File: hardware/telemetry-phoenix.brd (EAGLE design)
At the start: 100 x 80 mm, 134 parts, among them IC1 COPERNICUSSMD, IC10 TPS70933, IC2 TPS70933, IC4 STM32L052C8T6, IC5 TPS62160, IC6 HX1, IC7 LMP7702, IC8 ADXL345, J1 I2C1, J11 DNP, J13 LORA, J2 RASPBERRYPI-GPIOPTH, J5 BAT, J6 SMA_EDGE, J7 SMA_EDGE, J8 TEMP_E, Q1 SI4202DY, U1 VN5160S-E, U2 BME280, U3 VN5160S-E, Y1 32768, Y2 8M

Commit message: Add Phoenix telemetry PCB
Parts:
- removed C15, C27, C35: 1u, SparkFun-Passives:0805
- removed C17, C30: 0.1u, SparkFun-Passives:0805
- removed IC1: COPERNICUSSMD, SparkFun-RF:COPERNICUS
- removed J1: I2C1, SparkFun-Connectors:1X04_NO_SILK
- removed J13: LORA, HAB:1X08-2MM
- removed J5: BAT, SparkFun-Connectors:1X02
- removed J7: SMA_EDGE, SparkFun-Connectors:SMA-EDGE
- removed J8: TEMP_E, SparkFun-Connectors:JST-3-PTH
- removed JP1: GND, SparkFun-Passives:PAD-JUMPER-2-NC_BY_TRACE_YES_SILK
- removed OK1, OK2, OK3: LTV826S, optocoupler:DIL8-SMD
- removed R10\, R40: 430K, SparkFun-Passives:0805
- removed R2: 10K, SparkFun-Passives:0603-ARV
- removed R24, R42: 10K, SparkFun-Passives:0805
- removed R31, R33, R34, R35, R36, R37, R38, R39: 4.7K, SparkFun-Passives:0805
- removed R41: 100K, SparkFun-Passives:0805
- removed U1, U3: VN5160S-E, HAB:SO8
- removed U2: BME280, BME280ComponentLibrary:BME280_LGA
- added D11: 5.6V, SparkFun-DiscreteSemi:SOD-323
- added D15: 15V, SparkFun-DiscreteSemi:SOD-323
- added IC11, IC9: VN5160S-E, HAB:SO8
- added IC3: BME280, BME280ComponentLibrary:BME280_LGA
- added J3: POWER, HAB:1X10_SCREW
- added J4: GPS2, SparkFun-Connectors:1X06-1MM
- added J9: IO, SparkFun-Connectors:2X8
- added R56: 470K, SparkFun-Passives:0805
- D12: value 15V -> 5.6V
- J2: value RASPBERRYPI-GPIOPTH -> RASPBERRYPI-GPIO; device SparkFun-Boards:2X13-SHROUDED -> HAB:2X13-PI
- R10: value 470K -> 430K
- R21, R29, R30: value 4.7K -> 100
- R25, R4: value 10K -> 100
- R27: value 330k -> 330K
- R28: value 0 -> 100
- R32: value 4.7K -> DNP
- Y2: device SparkFun-FreqCtrl:HC49UP -> SparkFun-FreqCtrl:CRYSTAL-TXC-7A
- moved R50 277.0 mm to (53.3, 36.8)
- moved C29 257.0 mm to (46.4, 27.3), turned to 180 degrees
- moved R48 253.2 mm to (24.1, 40.0), turned to 180 degrees
- moved D13 252.9 mm to (54.6, 46.4), turned to 180 degrees
- moved R49 248.3 mm to (27.3, 26.7), turned to 180 degrees
- moved R51 247.7 mm to (4.45, 40.0)
- moved FRAME3 246.2 mm to (2.54, 57.1)
- moved C28 244.9 mm to (7.62, 48.9)
- moved R46 244.0 mm to (47.0, 52.7), turned to 180 degrees
- moved R47 243.9 mm to (47.0, 48.9), turned to 180 degrees
- moved R44 237.5 mm to (47.0, 50.8)
- moved R45 237.2 mm to (47.0, 47.0)
- moved Q1 235.2 mm to (53.3, 50.2), turned to 270 degrees
- moved R43 209.3 mm to (20.3, 48.3), turned to 270 degrees
- moved D12 190.5 mm to (12.7, 3.81), turned to 90 degrees
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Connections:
- net N$1 renamed CRB
- net N$2 renamed ACB
- removed net 15V: C29.1, R40.2, U3.5, U3.8
- removed net AGND: IC1.2, IC1.4, J7.GND@0, J7.GND@1, J7.GND@2, J7.GND@3, JP1.1
- removed net GPSBOOT: IC1.10, R4.1
- removed net L1+: R29.2
- removed net L1-: OK1.2
- removed net L2+: R31.2
- removed net L2-: OK2.2
- removed net L3+: R33.2
- removed net L3-: OK3.2
- removed net L4: OK1.3, R35.1
- removed net L4+: R35.2
- removed net L4-: OK1.4
- removed net L5: OK2.3, R37.1
- removed net L5+: R37.2
- removed net L5-: OK2.4
- removed net L6: OK3.3, R39.1
- removed net L6+: R39.2
- removed net L6-: OK3.4
- removed net LED4: IC4.28, OK1.6, R34.1
- removed net LED5: IC4.29, OK2.6, R36.1
- removed net LED6: IC4.32, OK3.6, R38.1
- removed net LP-: IC7.6, R28.1
- removed net PPS: IC1.19
- removed net RF_GPS: IC1.3, J7.SIG
- removed net RXA: IC1.21, R2.7
- removed net TXA: IC1.23, R2.6
- removed net VRAD: IC4.11, R40.1, R41.2
- removed net XRESET: IC1.11, R24.2
- removed net XSTBY: IC1.16, IC4.20, R25.2
- new net +9V: J3.6, J3.7, J3.8
- new net 3V_PI: J2.1
- new net 3V_PI2: J2.17
- net 15V_OUT: now also IC11.6, IC11.7, J3.4; no longer U3.6, U3.7
- net 3.3V: now also D12.C, J9.7, J9.8; no longer C11.1, C12.1, C15.1, C16.1, D10.C, IC1.12, J1.2, J13.7, J13.8, J2.1, J2.17, R2.2, R2.3, R2.4, R21.2, R24.1, R25.1, R30.2, R34.2, R36.2, R38.2, R4.2, R42.2, U2.P$2, U2.P$6, U2.P$8
- net 5V: now also IC9.5, IC9.8, J4.2, R10.2; no longer C17.1, R10\.2, U1.5, U1.8
- net 5V_PI: now also IC9.6, IC9.7; no longer C27.1, U1.6, U1.7
- net A-: now also R56.2; no longer R10.2
- net ALT_CTRL: now also J3.9
- net BME_SDO: now also IC3.P$5; no longer U2.P$5
- net B_LORA: now also D10.C, J9.14; no longer J13.3
- net B_MISO: now also J9.10, R28.1; no longer J13.6
- net B_MOSI: now also J9.6, R25.1; no longer J13.2
- net B_SCK: now also J9.12, R4.1; no longer J13.4
- net CUT_ROPE: now also D15.C, J3.10; no longer D12.C
- net D_PI: now also IC9.4; no longer U1.4
- net D_RAD: now also IC11.4; no longer U3.4
- net FB5: now also R10.1; no longer R10\.1
- net GND: now also D11.A, D15.A, IC11.1, IC3.P$1, IC3.P$7, IC9.1, J3.2, J3.3, J3.5, J4.1, J4.5, J9.15, J9.16, J9.9, R56.1; no longer C11.2, C12.2, C15.2, C17.2, C27.2, C30.2, C35.2, IC1.1, IC1.13, IC1.14, IC1.15, IC1.27, IC1.28, J1.1, J13.1, J13.5, J5.1, J8.2, JP1.2, OK1.5, OK1.7, OK2.5, OK2.7, OK3.5, OK3.7, R10.1, R41.1, U1.1, U2.P$1, U2.P$7, U3.1
- net GPSRX: no longer IC1.24, R2.5
- net GPSRX2: now also J4.4
- net GPSTX: no longer IC1.20
- net GPSTX2: now also J4.3
- net K_PI: now also IC4.10, IC9.2; no longer IC4.15, U1.2
- net K_RAD: now also IC11.2, IC4.29; no longer IC4.13, U3.2
- net L1: now also J9.2, R21.1; no longer OK1.1, R29.1
- net L2: now also J9.1, R29.1; no longer OK2.1, R31.1
- net L3: now also J9.4, R30.1; no longer OK3.1, R33.1
- net LED1: now also IC4.13, R21.2; no longer IC4.25, OK1.8, R21.1
- net LED2: now also IC4.12, R29.2; no longer IC4.26, OK2.8, R30.1
- net LED3: now also IC4.11, R30.2; no longer IC4.27, OK3.8, R32.1
- net LS1: now also J2.22; no longer J2.18
- net LS2: now also J2.18; no longer J2.22
- net MISO: now also R28.2
- net MOSI: now also R25.2
- net OSC_IN: now also Y2.P$1; no longer Y2.1
- net OSC_OUT: now also Y2.P$2; no longer Y2.2
- net R_TX: no longer R42.1
- net SCK: now also R4.2
- net SCL: now also IC3.P$4, J9.5; no longer J1.4, U2.P$4
- net SDA: now also IC3.P$3, J9.3; no longer J1.3, U2.P$3
- net TEMP: now also IC4.28, J9.13, R32.1; no longer IC4.10, J8.3
- net TXD: now also IC7.6; no longer R28.2
- net VBAT: now also C29.1, IC11.5, IC11.8, J3.1; no longer J5.2
- net VDIV: now also IC4.15; no longer IC4.12
- net VS: now also C16.1, D11.C, IC3.P$2, IC3.P$6, IC3.P$8, J9.11; no longer C30.1, C35.1, J8.1
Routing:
- net 3.3V: track 0.00 -> 93.1 mm
- net SCL: track 0.00 -> 78.1 mm, vias 0 -> 4
- net SDA: track 0.00 -> 77.5 mm, vias 0 -> 3
- net VS: track 0.00 -> 62.2 mm
- net K_RAD: track 0.00 -> 48.1 mm, vias 0 -> 2
- net !RST!: track 0.00 -> 40.2 mm, vias 0 -> 2
- net R_RX: track 0.00 -> 38.5 mm, vias 0 -> 1
- net LED2: track 0.00 -> 34.1 mm, vias 0 -> 2
- net GPSRX2: track 0.00 -> 33.8 mm, vias 0 -> 2
- net TEMP: track 0.00 -> 33.5 mm, vias 0 -> 2
- net K_PI: track 0.00 -> 33.4 mm, vias 0 -> 2
- net LED1: track 0.00 -> 33.2 mm, vias 0 -> 2
- net LED3: track 0.00 -> 33.1 mm, vias 0 -> 2
- net GPSTX2: track 0.00 -> 32.9 mm, vias 0 -> 2
- net MOSI: track 0.00 -> 30.7 mm, vias 0 -> 2
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- added copper zone on layer 1, net 15V_OUT
- added copper zone on layer 1, net 3.3V
- added copper zone on layer 1, net 5V
- added copper zone on layer 16, net 5V
- added copper zone on layer 1, net 5V_PI
- added copper zone on layer 1, net ALT_CTRL
- added copper zone on layer 1, net CUT_ROPE
- added copper zone on layer 1, net GND
- added copper zone on layer 16, net GND
- added copper zone on layer 1, net RGND
- added copper zone on layer 16, net RGND
- added copper zone on layer 1, net SW5
- added copper zone on layer 1, net VBAT
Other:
- board size 100 x 80 mm -> 65 x 56 mm

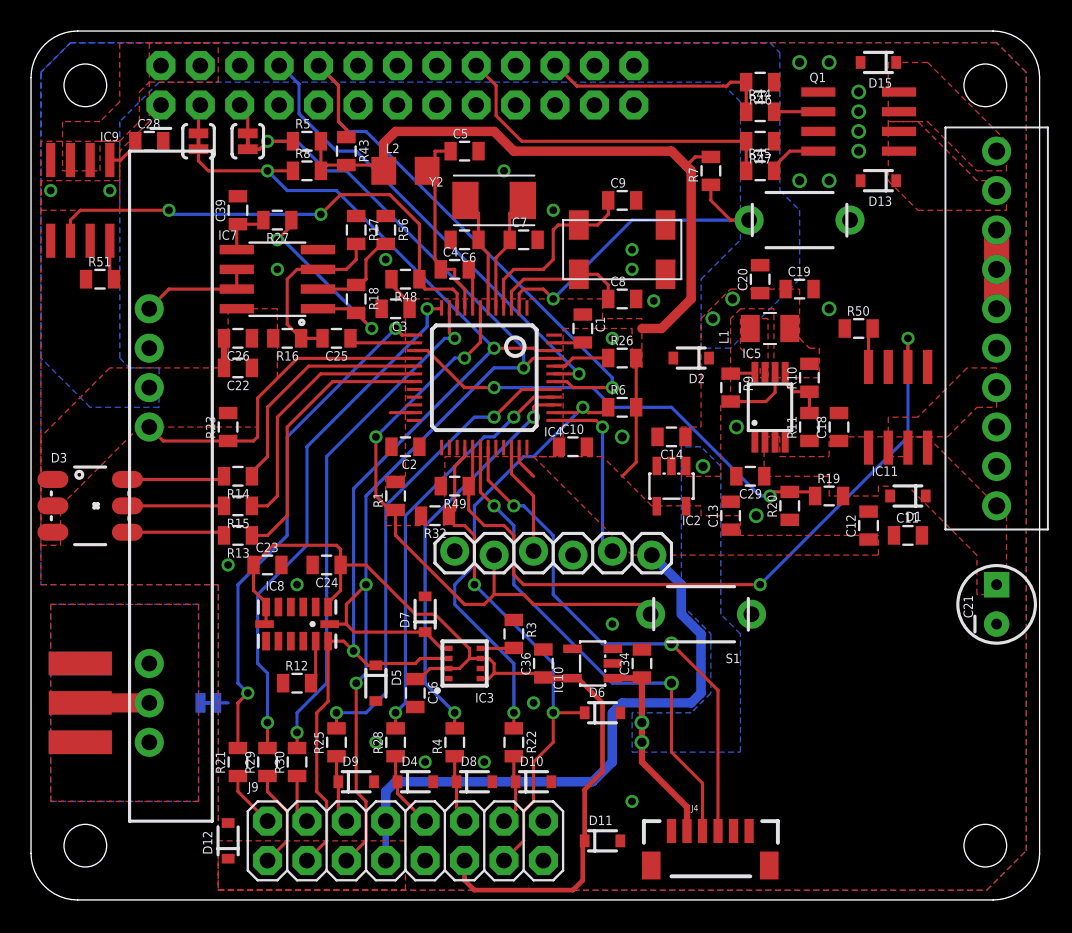
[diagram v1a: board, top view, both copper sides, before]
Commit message: Add GPS1 connector to Phoenix board
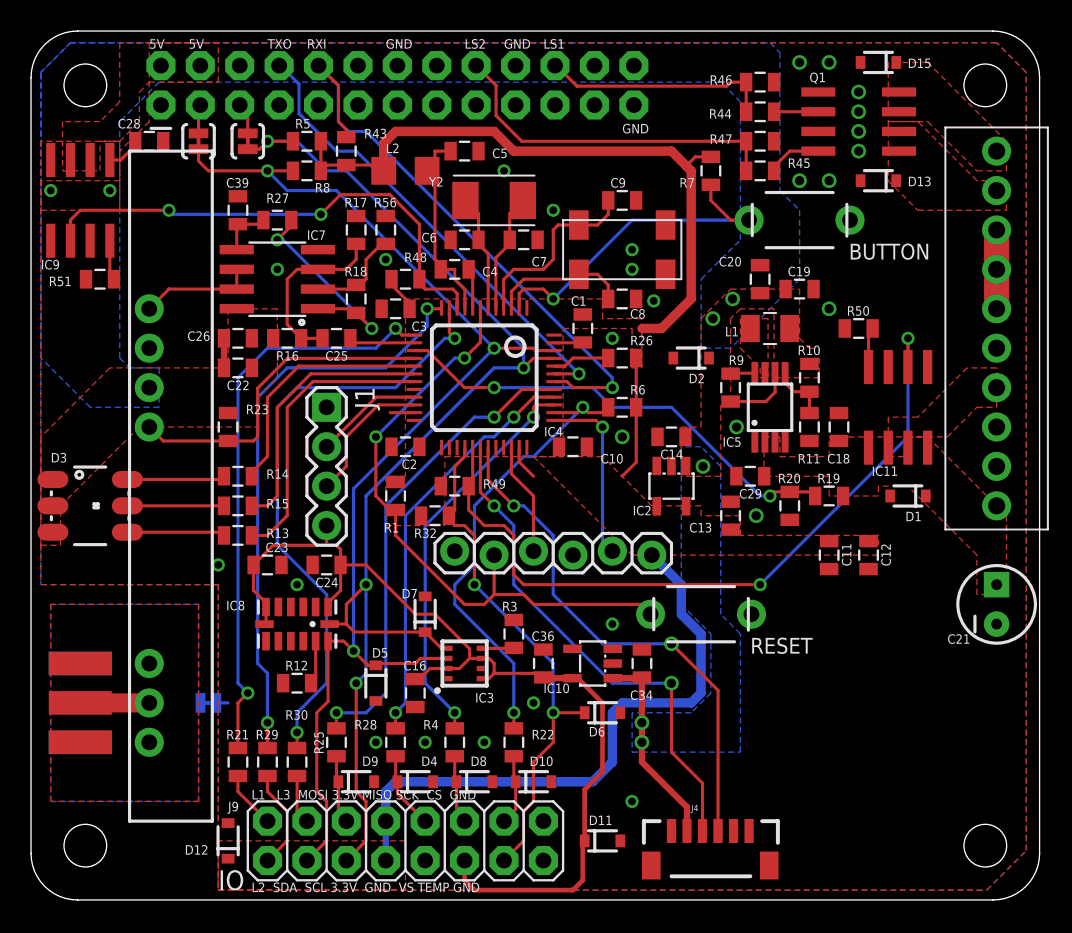
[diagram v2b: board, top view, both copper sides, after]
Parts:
- removed FRAME3: FRAME-LETTERNO_PACKAGE, SparkFun-Aesthetics:DUMMY
- added J1: GPS1, SparkFun-Connectors:1X04
- R56: value 470K -> 430K
- moved C11 5.24 mm to (51.4, 22.2), turned to 270 degrees
- moved C12 1.90 mm to (54.0, 22.2), turned to 270 degrees
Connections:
- net 3.3V: now also C11.1, C12.1
- net GND: now also C11.2, C12.2, J1.1
- net GPSRX: now also J1.3
- net GPSTX: now also J1.2
- net VS: now also J1.4
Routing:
- net GPSRX: track 0.00 -> 8.94 mm
- net GPSTX: track 0.00 -> 6.98 mm
- net LED3: track 33.1 -> 39.4 mm
- net LED1: track 33.2 -> 37.3 mm
- net LED2: track 34.1 -> 37.8 mm
- net VS: track 62.2 -> 63.5 mm
- net LEDB: track 17.9 -> 18.7 mm
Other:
- board text added: "5V"
- board text added: "BUTTON"
- board text added: "GND"
- board text added: "L1 L3 MOSI 3.3V MISO SCK CS GND"
- board text added: "L2 SDA SCL 3.3V GND VS TEMP GND"
- board text added: "LS1"
- board text added: "LS2"
- board text added: "RESET"
- board text added: "RXI"
- board text added: "TXO"

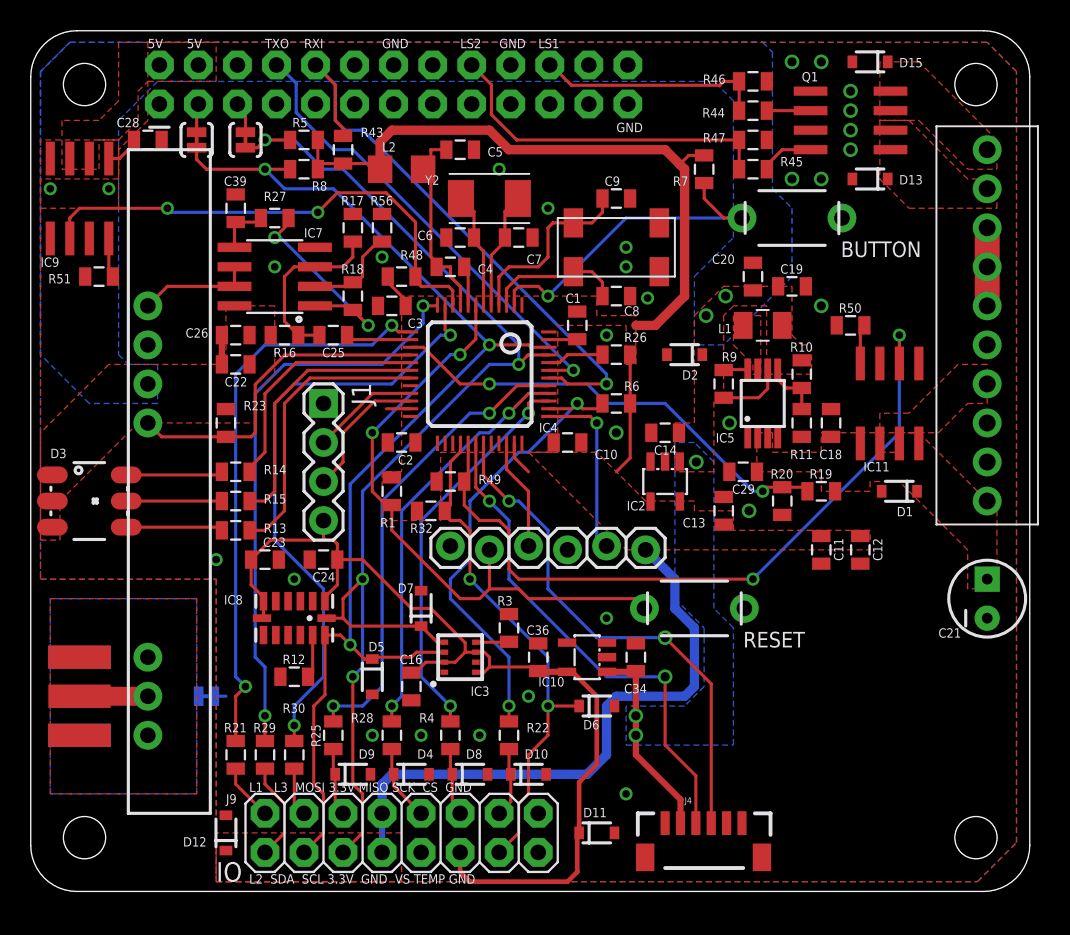
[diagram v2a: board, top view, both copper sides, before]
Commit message: Rotate and reroute Phoenix board, much cleaner!
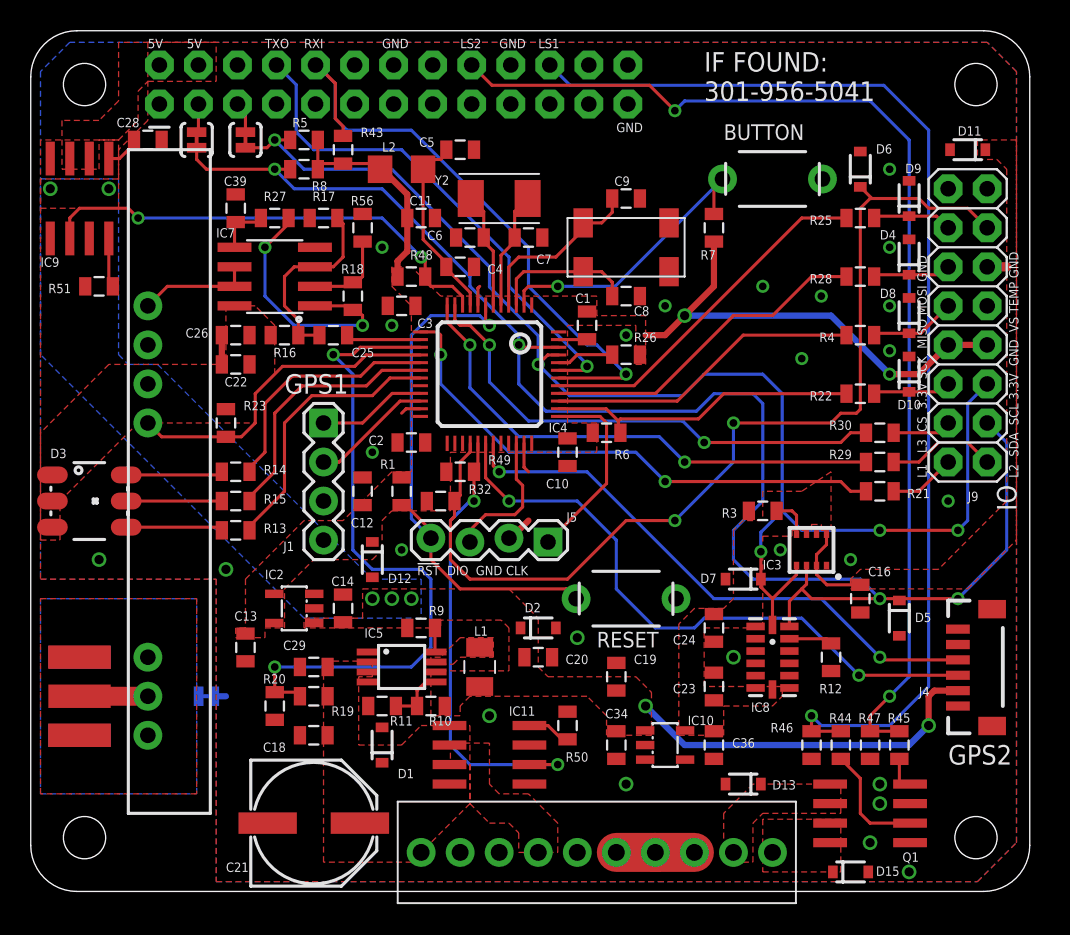
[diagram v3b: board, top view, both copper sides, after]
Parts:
- removed J11: DNP, SparkFun-Connectors:1X06_LOCK
- added J5: DNP, SparkFun-Connectors:1X04_LOCK
- added U$1: (no value), HAB:GARAGE
- added U$2: (no value), HAB:MSFT_LOGO
- C21: device SparkFun-Passives:CPOL-RADIAL-10UF-25V -> SparkFun-Passives:PANASONIC_E
- moved J9 53.4 mm to (62.2, 27.9), turned to 90 degrees
- moved D15 52.7 mm to (53.3, 1.27), turned to 0 degrees
- moved D9 52.1 mm to (57.1, 45.1), turned to 90 degrees
- moved D11 50.6 mm to (61.0, 48.3), turned to 180 degrees
- moved R25 48.0 mm to (54.0, 43.8), turned to 180 degrees
- moved D4 46.7 mm to (57.1, 41.3), turned to 90 degrees
- moved C21 46.2 mm to (18.4, 4.45), turned to 0 degrees
- moved R21 45.3 mm to (55.2, 26.0), turned to 180 degrees
- moved Q1 45.1 mm to (54.6, 5.08), turned to 90 degrees
- moved R29 44.3 mm to (55.2, 27.9), turned to 180 degrees
- moved R30 43.5 mm to (55.2, 29.8), turned to 180 degrees
- moved R46 43.3 mm to (50.8, 9.53), turned to 90 degrees
- moved J3 43.3 mm to (25.4, 2.54), turned to 0 degrees
- moved R28 42.7 mm to (54.0, 40.0), turned to 180 degrees
- moved R44 41.7 mm to (52.7, 9.53), turned to 270 degrees
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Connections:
- net !RST!: now also J5.4; no longer J11.5
- net 3.3V: now also J1.4; no longer J11.1
- net B_LORA: now also J9.6; no longer J9.14
- net B_MISO: now also J9.12; no longer J9.10
- net B_MOSI: now also J9.14; no longer J9.6
- net B_SCK: now also J9.10; no longer J9.12
- net GND: now also C21.-, J1.3, J5.2; no longer C21.2, J1.1, J11.3
- net GPSRX: now also J1.2; no longer J1.3
- net GPSTX: now also J1.1; no longer J1.2
- net SWCLK: now also J5.1; no longer J11.2
- net SWDIO: now also J5.3; no longer J11.4
- net VBAT: now also C21.+; no longer C21.1
- net VS: no longer J1.4
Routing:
- net LS1: track 14.9 -> 74.4 mm, vias 0 -> 1
- net VS: track 63.5 -> 7.29 mm
- net LS2: track 22.5 -> 72.4 mm, vias 0 -> 2
- net 3.3V: track 93.1 -> 45.0 mm, vias 0 -> 2
- net TEMP: track 33.5 -> 64.8 mm
- net SDA: track 77.5 -> 100.8 mm, vias 3 -> 4
- net K_RAD: track 48.1 -> 29.9 mm
- net VDIV: track 29.9 -> 43.5 mm
- net SCL: track 78.1 -> 88.6 mm, vias 4 -> 5
- net CS: track 30.0 -> 20.6 mm, vias 2 -> 0
- net GPSTX2: track 32.9 -> 40.7 mm
- net MOSI: track 30.7 -> 23.2 mm, vias 2 -> 0
- net LED3: track 39.4 -> 32.7 mm
- net 5V: track 19.6 -> 26.3 mm
- net SCK: track 25.8 -> 20.5 mm, vias 2 -> 0
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- added copper zone on layer 1, net VS
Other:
- board text added: "!RST! DIO GND CLK"
- board text added: "301-956-5041"
- board text added: "IF FOUND:"
- board text added: "L1 L3 CS 3.3V SCK MISO MOSI GND"
- board text added: "Make it your pastime Make it your mission Go ECE!"
- board text added: "Microsoft Maker Garage"
- board text added: "Project Phoenix"
- board text added: "REV A"
- board text removed: "L1 L3 MOSI 3.3V MISO SCK CS GND"
